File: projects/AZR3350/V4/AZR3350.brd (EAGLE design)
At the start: 80.5 x 141.4 mm, 194 parts, among them IC1 LM2734Y, IC10 A4988, IC2 LDO-TS1117CW-3V3, IC3 ATSAM4S8C, IC4 SI87XXIS, IC5 74HC125, IC6 74S08D, IC7 A4988, IC8 A4988, IC9 A4988, J1 ZX62-AB-5PA, J3 MSTBV4, J4 MOLEX-105162-001, Q1 NX138BKS, Q2 BUK9Y53-100B, Q3 BUK9Y53-100B, Q4 BC817-16SMD, X1 12MHz

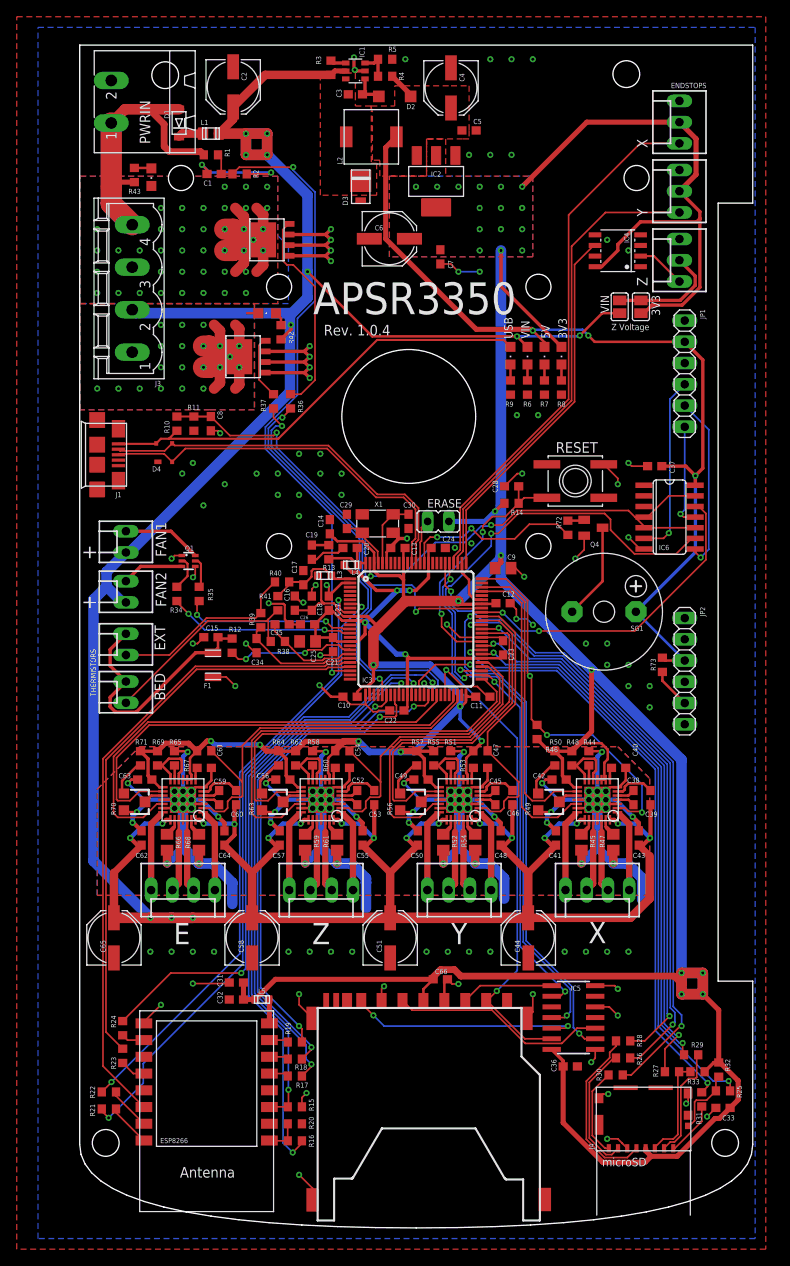
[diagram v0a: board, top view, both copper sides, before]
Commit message: Replacing .35mm vias with .4mm
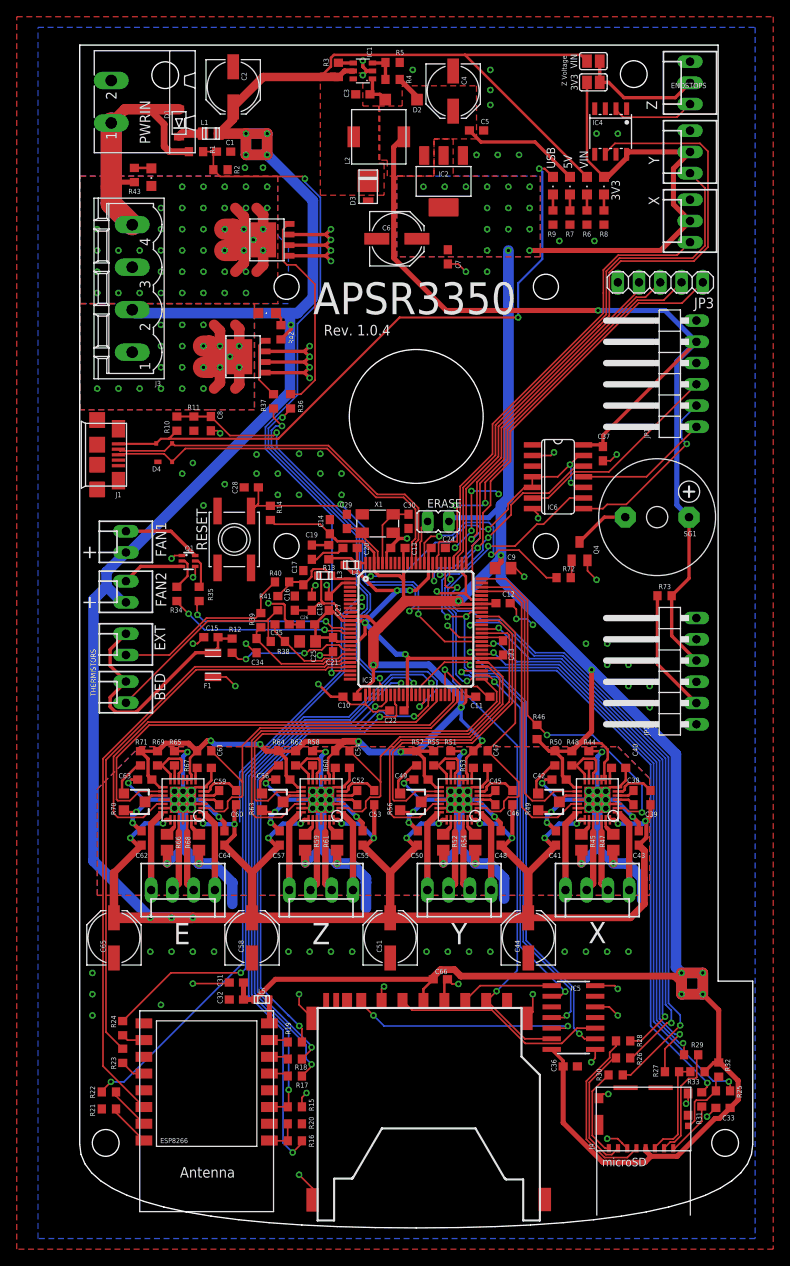
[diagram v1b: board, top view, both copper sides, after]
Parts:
- added JP3: (no value), pinhead:1X05
- JP1, JP2: device pinhead:1X06 -> pinhead:1X06/90
- moved RESET 41.4 mm to (114.2, 82.3), turned to 270 degrees
- moved C28 31.1 mm to (116.2, 88.5)
- moved SJ2 29.5 mm to (157.1, 139.5), turned to 0 degrees
- moved R14 28.8 mm to (118.5, 85.5), turned to 270 degrees
- moved SJ1 27.4 mm to (157.1, 136.9), turned to 0 degrees
- moved R6 21.5 mm to (156.3, 120.8)
- moved VIN 21.5 mm to (156.3, 124.6)
- moved Z_STOP 21.2 mm to (168.7, 136.9)
- moved 3V3 20.9 mm to (158.4, 124.6)
- moved R8 20.9 mm to (158.4, 120.8)
- moved R9 20.9 mm to (152.3, 120.8)
- moved USB 20.9 mm to (152.3, 124.6)
- moved 5V 20.5 mm to (154.3, 124.6)
- moved R7 20.5 mm to (154.3, 120.8)
- moved IC4 14.3 mm to (159.2, 131.1), turned to 180 degrees
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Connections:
- removed net LCD_RST: IC3.84
- new net LCD_KILL: IC3.84, JP3.4
- net +5V: now also JP1.5, JP2.4; no longer JP1.2, JP2.3
- net BTN_EN1: now also JP3.1
- net BTN_EN2: now also JP3.2
- net BTN_ENC: now also JP3.3
- net GND: now also JP1.6, JP3.5; no longer JP1.1
- net LCD_CS_BUF: now also JP1.3; no longer JP1.4
- net LCD_MOSI_BUF: now also JP1.2; no longer JP1.5
- net LCD_SCK_BUF: now also JP1.1; no longer JP1.6
- net N$2: now also JP2.2; no longer JP2.5
- net RESET: now also RESET.A; no longer RESET.A'
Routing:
- net BTN_EN1: track 0.00 -> 53.6 mm, vias 0 -> 2
- net LCD_KILL: track 0.00 -> 51.7 mm, vias 0 -> 2
- net BTN_EN2: track 0.00 -> 50.9 mm, vias 0 -> 2
- net BTN_ENC: track 0.00 -> 48.3 mm
- net URXD1: track 76.5 -> 35.1 mm, vias 2 -> 1
- net Z_STOP: track 44.4 -> 80.1 mm
- net +3V3: track 526.0 -> 500.9 mm, vias 30 -> 29
- net VBUS: track 53.7 -> 76.6 mm, vias 0 -> 2
- net +5V: track 112.7 -> 134.2 mm, vias 3 -> 1
- net LCD_MOSI: track 96.2 -> 79.5 mm
- net LCD_CS: track 52.9 -> 38.5 mm, vias 2 -> 4
- net RESET: track 30.9 -> 43.4 mm
- net +24V: track 424.2 -> 435.3 mm, vias 27 -> 24
- net N$2: track 4.82 -> 14.8 mm
- net X_STOP: track 64.1 -> 54.2 mm
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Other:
- outline, holes or cut-outs redrawn

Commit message: Not exactly sure what I changed
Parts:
- moved C23 0.13 mm to (146.4, 69.3)
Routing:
- net URXD1: track 35.1 -> 79.4 mm, vias 1 -> 2
- net LCD_KILL: track 51.7 -> 49.3 mm
- net GND: track 466.7 -> 469.0 mm
- net +24V: track 435.3 -> 436.3 mm
- net BEEPER: track 24.7 -> 25.5 mm
- net PWR_FAIL_DET: track 83.5 -> 84.2 mm
- net LCD_SCK: track 92.4 -> 93.1 mm
- net MCCDA: track 66.4 -> 67.0 mm

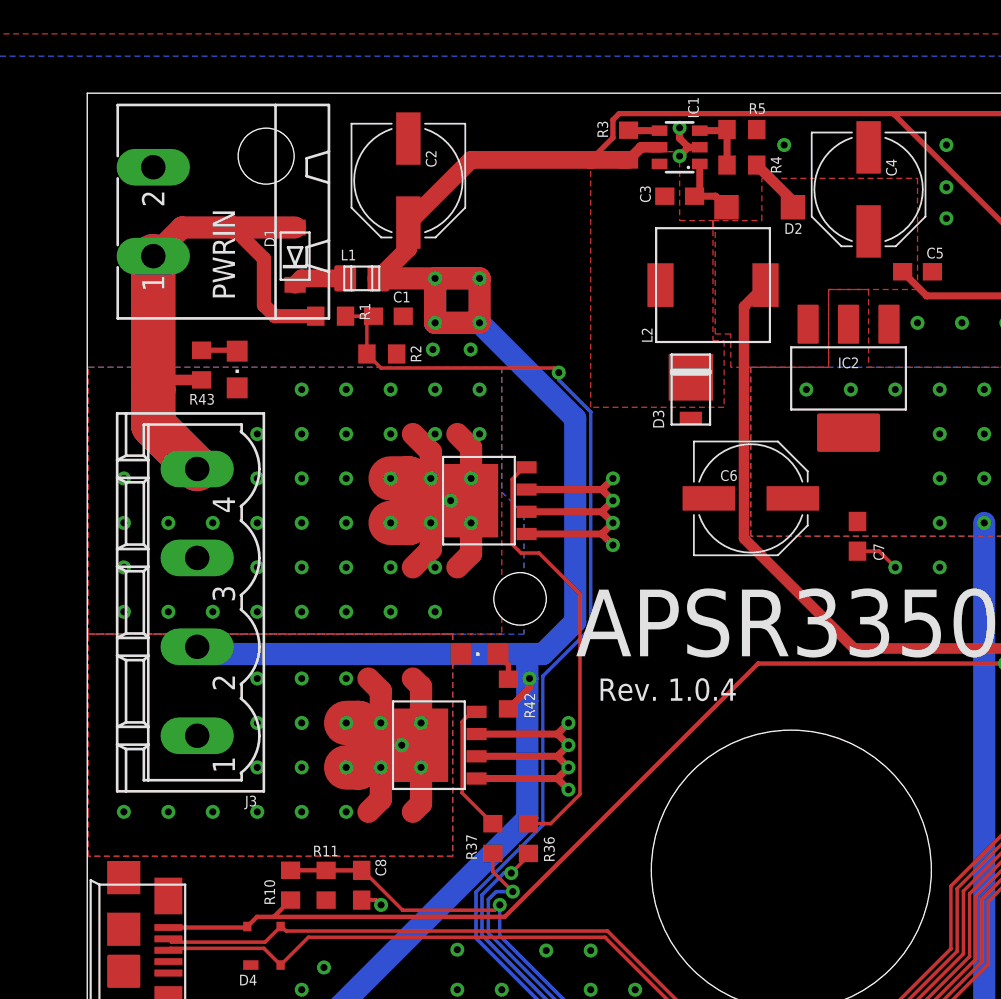
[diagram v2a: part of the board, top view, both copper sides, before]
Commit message: New 32-bit AMR3350 (probably will be renamed), + other edits
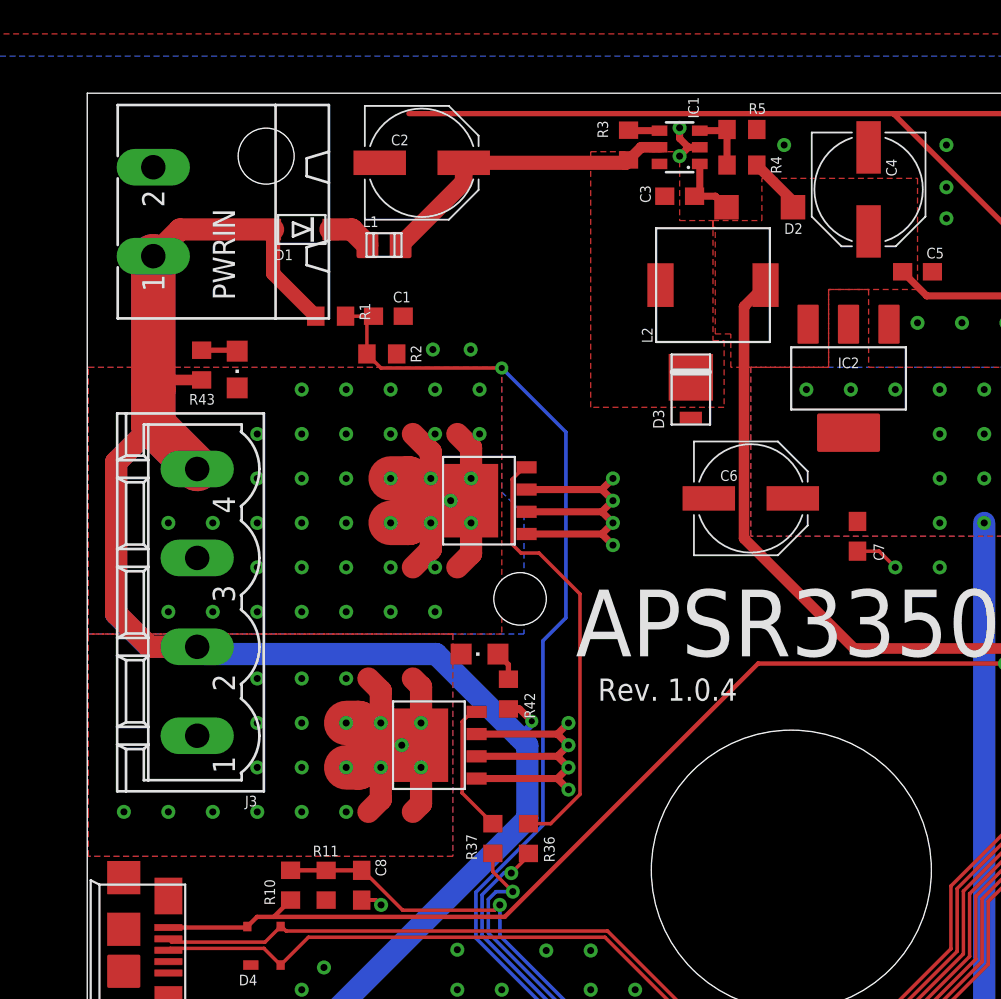
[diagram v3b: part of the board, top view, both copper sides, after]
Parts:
- moved L1 2.29 mm to (112.7, 132.7)
- moved D1 1.57 mm to (108.0, 133.6), turned to 180 degrees
- moved C2 1.27 mm to (114.8, 137.4), turned to 0 degrees
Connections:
- removed net VIN: D1.A, J3.4, PWRIN.1, R1.2, R43.2
- new net N$3: C2.+, IC1.5, L1.2, R3.1
- net +24V: now also D1.A, J3.4, PWRIN.1, R1.2, R43.2; no longer C2.+, IC1.5, L1.2, R3.1
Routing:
- net VIN: track 46.6 -> 0.00 mm
- net N$3: track 0.00 -> 17.7 mm
- net +24V: track 436.3 -> 451.1 mm, vias 24 -> 20
- net PWR_FAIL_DET: track 84.2 -> 81.2 mm
- net VIN_F: track 3.01 -> 2.48 mm
- net BED_D: vias 42 -> 38

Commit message: A few small changes
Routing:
- net +24V: track 451.1 -> 462.2 mm
- net GND: track 469.0 -> 466.7 mm, vias 170 -> 172
- net MCCDA: track 67.0 -> 66.4 mm

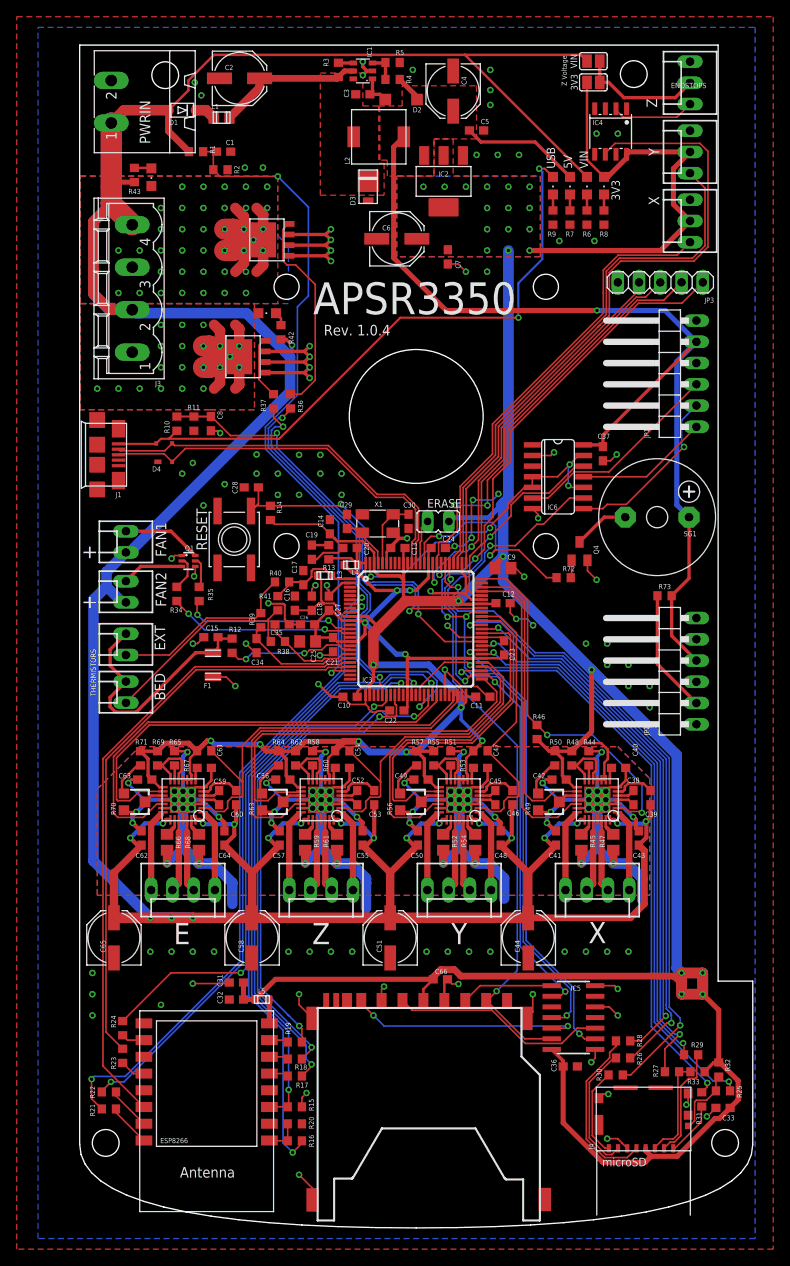
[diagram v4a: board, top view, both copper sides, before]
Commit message: Changes from a while back, which I think involved a different component choice?
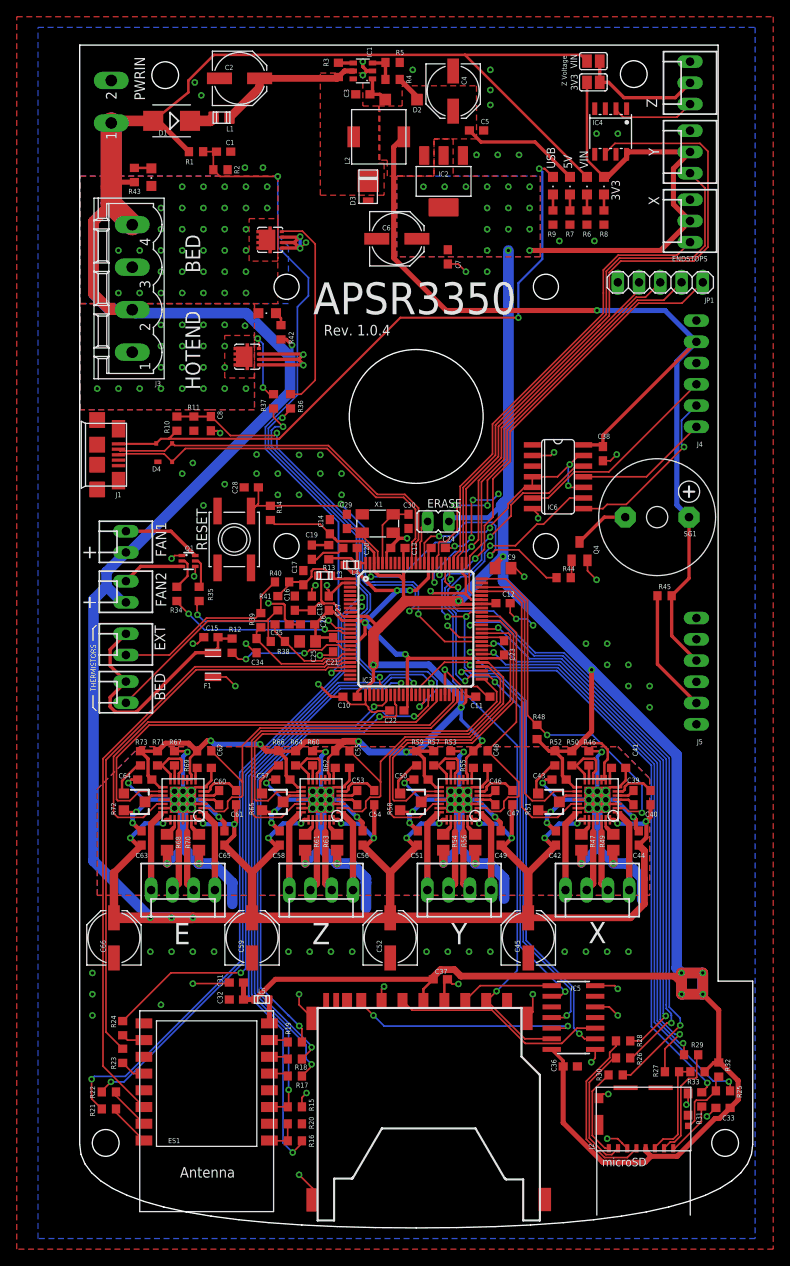
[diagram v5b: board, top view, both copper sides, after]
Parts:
- removed JP2: (no value), pinhead:1X06/90
- removed JP3: (no value), pinhead:1X05
- added J2: MOLEX-105162-001, misc:MOLEX-105162
- added J5: (no value), con-other:1X06/90
- C37: value 100n -> 1u
- C40, C42, C47, C49, C54, C56, C61, C63: value 220n -> 100n
- C41, C43, C48, C50, C55, C57, C62, C64: value 100n -> 220n
- C44, C51, C58, C65: value 100u -> 100n; device resistor:PANASONIC_D -> resistor:C0603
- C45, C52, C59: value 100n -> 100u; device resistor:C0603 -> resistor:PANASONIC_D
- C66: value 1u -> 100u; device resistor:C0603 -> resistor:PANASONIC_D
- D1: device adafruit:SOD-123FL -> diode:SMB
- J4: value MOLEX-105162-001 -> (none); device misc:MOLEX-105162 -> con-other:1X06/90
- JP1: device pinhead:1X06/90 -> pinhead:1X05
- PWRIN: value MSTBA2 -> 2-PIN-508; device con-phoenix-508:MSTBA2 -> con-other:2-PIN-508
- Q2, Q3: value BUK9Y53-100B -> AON7524; device misc:SOT-669 -> misc:3X3DFN-EP
- R44: value 10K -> 1K
- R45: value 0R2 -> 47R; device resistor:R0805 -> resistor:R0603
- R48, R55, R62, R69: value 100K -> 10K
- R49, R56, R63, R70: value 10K -> 0R2; device resistor:RTRIM3103 -> resistor:R0805
- R50, R57, R64, R71: value 20K -> 100K
- R51, R58, R65: device resistor:R0603 -> resistor:RTRIM3103
- R52, R59, R66: value 0R2 -> 20K; device resistor:R0805 -> resistor:R0603
- R72: value 1K -> 10K; device resistor:R0603 -> resistor:RTRIM3103
- R73: value 47R -> 20K
- moved J4 93.1 mm to (165.6, 102.1), turned to 90 degrees
- moved C37 65.8 mm to (138.8, 29.7), turned to 0 degrees
- moved R73 65.6 mm to (103.0, 56.1), turned to 90 degrees
- moved R72 57.9 mm to (102.2, 50.9), turned to 270 degrees
- moved C38 41.3 mm to (158.2, 92.5), turned to 270 degrees
- moved C66 39.3 mm to (99.8, 34.7), turned to 90 degrees
- moved R45 31.1 mm to (165.6, 75.6), turned to 180 degrees
- moved R44 21.8 mm to (153.5, 77.7), turned to 0 degrees
- moved C44 17.8 mm to (162.5, 46.6)
- moved C65 17.8 mm to (113.0, 46.6)
- moved C52 17.2 mm to (132.8, 34.7)
- moved C59 17.2 mm to (116.3, 34.7)
- moved C45 17.2 mm to (149.3, 34.7)
- moved R52 16.7 mm to (152.5, 56.1)
- moved R59 16.7 mm to (136.0, 56.1)
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- renumbered ESP8266 to ES1
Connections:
- net +24V: now also C40.2, C42.1, C44.1, C45.+, C47.2, C49.1, C51.1, C52.+, C54.2, C56.1, C58.1, C59.+, C61.2, C63.1, C65.1, C66.+; no longer C39.2, C41.1, C43.1, C44.+, C46.2, C48.1, C50.1, C51.+, C53.2, C55.1, C57.1, C58.+, C60.2, C62.1, C64.1, C65.+
- net +3V3: now also C37.1, C43.1, C50.1, C57.1, C64.1, J2.P4, R52.2, R59.2, R66.2, R73.2; no longer C42.1, C49.1, C56.1, C63.1, C66.1, J4.P4, R46.2, R53.2, R60.2, R67.2
- net +5V: now also C38.1, J4.5, J5.4, R45.1; no longer C37.1, JP1.5, JP2.4, R73.1
- net BED_D: now also Q3.5, Q3.6, Q3.7, Q3.8, Q3.E1, Q3.E2, Q3.PAD; no longer Q3.EXP, Q3.MB
- net BEEPER: now also R44.1; no longer R72.1
- net BTN_EN1: now also JP1.1; no longer JP3.1
- net BTN_EN2: now also JP1.2; no longer JP3.2
- net BTN_ENC: now also JP1.3; no longer JP3.3
- net CLK: now also J2.P5; no longer J4.P5
- net CMD: now also J2.P3; no longer J4.P3
- net CP1E: now also C60.1; no longer C59.1
- net CP1X: now also C39.1; no longer C38.1
- net CP1Y: now also C46.1; no longer C45.1
- net CP1Z: now also C53.1; no longer C52.1
- net CP2E: now also C60.2; no longer C59.2
- net CP2X: now also C39.2; no longer C38.2
- net CP2Y: now also C46.2; no longer C45.2
- net CP2Z: now also C53.2; no longer C52.2
- net DAT0: now also J2.P7; no longer J4.P7
- net DAT1: now also J2.P8; no longer J4.P8
- net DAT2: now also J2.P1; no longer J4.P1
- net DAT3: now also J2.P2; no longer J4.P2
- net DET: now also J2.P9; no longer J4.P9
- net EXT_D: now also Q2.5, Q2.6, Q2.7, Q2.8, Q2.E1, Q2.E2, Q2.PAD; no longer Q2.EXP, Q2.MB
- net E_EN: now also R69.1; no longer R67.1
- net GND: now also C38.2, C44.2, C45.-, C51.2, C52.-, C58.2, C59.-, C65.2, C66.-, J2.G1, J2.G2, J2.G3, J2.G4, J2.P6, J4.6, J5.1, J5.6, JP1.5, R46.2, R49.1, R51.3, R53.2, R56.1, R58.3, R60.2, R63.1, R65.3, R67.2, R70.1, R72.3; no longer C40.2, C44.-, C47.2, C51.-, C54.2, C58.-, C61.2, C65.-, C66.2, J4.G1, J4.G2, J4.G3, J4.G4, J4.P6, JP1.6, JP2.1, JP2.6, JP3.5, R44.2, R45.1, R49.3, R51.2, R52.1, R56.3, R58.2, R59.1, R63.3, R65.2, R66.1, R70.3
- net LCD_CS_BUF: now also J4.3; no longer JP1.3
- net LCD_KILL: now also JP1.4; no longer JP3.4
- net LCD_MOSI_BUF: now also J4.2; no longer JP1.2
- net LCD_SCK_BUF: now also J4.1; no longer JP1.1
- net N$2: now also J5.2, R45.2; no longer JP2.2, R73.2
- net N$7: now also R44.2; no longer R72.2
- net REFE: now also R72.2; no longer R70.2
- net REFE-IN: now also R72.1, R73.1; no longer R70.1, R71.1
- net REFX: now also R51.2; no longer R49.2
- net REFX-IN: now also R51.1, R52.1; no longer R49.1, R50.1
- net REFY: now also R58.2; no longer R56.2
- net REFY-IN: now also R58.1, R59.1; no longer R56.1, R57.1
- net REFZ: now also R65.2; no longer R63.2
- net REFZ-IN: now also R65.1, R66.1; no longer R63.1, R64.1
- net ROSCE: now also R67.1; no longer R65.1
- net ROSCX: now also R46.1; no longer R44.1
- net ROSCY: now also R53.1; no longer R51.1
- net ROSCZ: now also R60.1; no longer R58.1
- net RSTE: now also R71.1; no longer R69.1
- net RSTX: now also R50.1; no longer R48.1
- net RSTY: now also R57.1; no longer R55.1
- net RSTZ: now also R64.1; no longer R62.1
- net SNS1E: now also R68.2; no longer R66.2
- net SNS1X: now also R47.2; no longer R45.2
- net SNS1Y: now also R54.2; no longer R52.2
- net SNS1Z: now also R61.2; no longer R59.2
- net SNS2E: now also R70.2; no longer R68.2
- net SNS2X: now also R49.2; no longer R47.2
- net SNS2Y: now also R56.2; no longer R54.2
- net SNS2Z: now also R63.2; no longer R61.2
- net VCPE: now also C61.1; no longer C60.1
- net VCPX: now also C40.1; no longer C39.1
- net VCPY: now also C47.1; no longer C46.1
- net VCPZ: now also C54.1; no longer C53.1
- net VREGE: now also C62.1; no longer C61.1
- net VREGX: now also C41.1; no longer C40.1
- net VREGY: now also C48.1; no longer C47.1
- net VREGZ: now also C55.1; no longer C54.1
- net X_EN: now also R48.1; no longer R46.1
- net Y_EN: now also R55.1; no longer R53.1
- net Z_EN: now also R62.1; no longer R60.1
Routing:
- net BED_D: track 22.4 -> 0.00 mm, vias 38 -> 35
- net EXT_D: track 21.2 -> 0.00 mm, vias 20 -> 21
- net GND: track 466.7 -> 456.5 mm, vias 172 -> 169
- net EXT_G: track 7.62 -> 8.97 mm, vias 0 -> 2
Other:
- board text added: "BED"
- board text added: "HOTEND"

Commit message: Ulticontroller adapter, AZR stuff?
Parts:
- moved R14 1.27 mm to (119.3, 86.5), turned to 0 degrees
- moved IC6 0.25 mm to (152.9, 90.0)
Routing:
- net USB_PWR_MON: track 53.4 -> 56.5 mm
- net VBUS: track 76.6 -> 79.5 mm
- net PWR_FAIL_DET: track 81.2 -> 79.6 mm, vias 2 -> 3
- net GND: track 456.5 -> 458.0 mm, vias 169 -> 171
- net HOTEND: track 52.9 -> 54.1 mm
- net LCD_MOSI: track 80.0 -> 80.9 mm
- net Z_STOP: track 80.1 -> 79.6 mm
- net +3V3: track 500.7 -> 500.9 mm, vias 29 -> 28
